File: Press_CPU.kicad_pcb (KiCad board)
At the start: 6 copper layers, 38.5 x 33 mm, 98 parts, among them J2 2-215079-0, J3 Conn_01x16, J4 Conn_01x16, U1 APM32F405RGT6, U10 LMV321, U11 LMV321, U12 FM25W256, U13 LMV321, U14 LMV321, U15 LMV321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

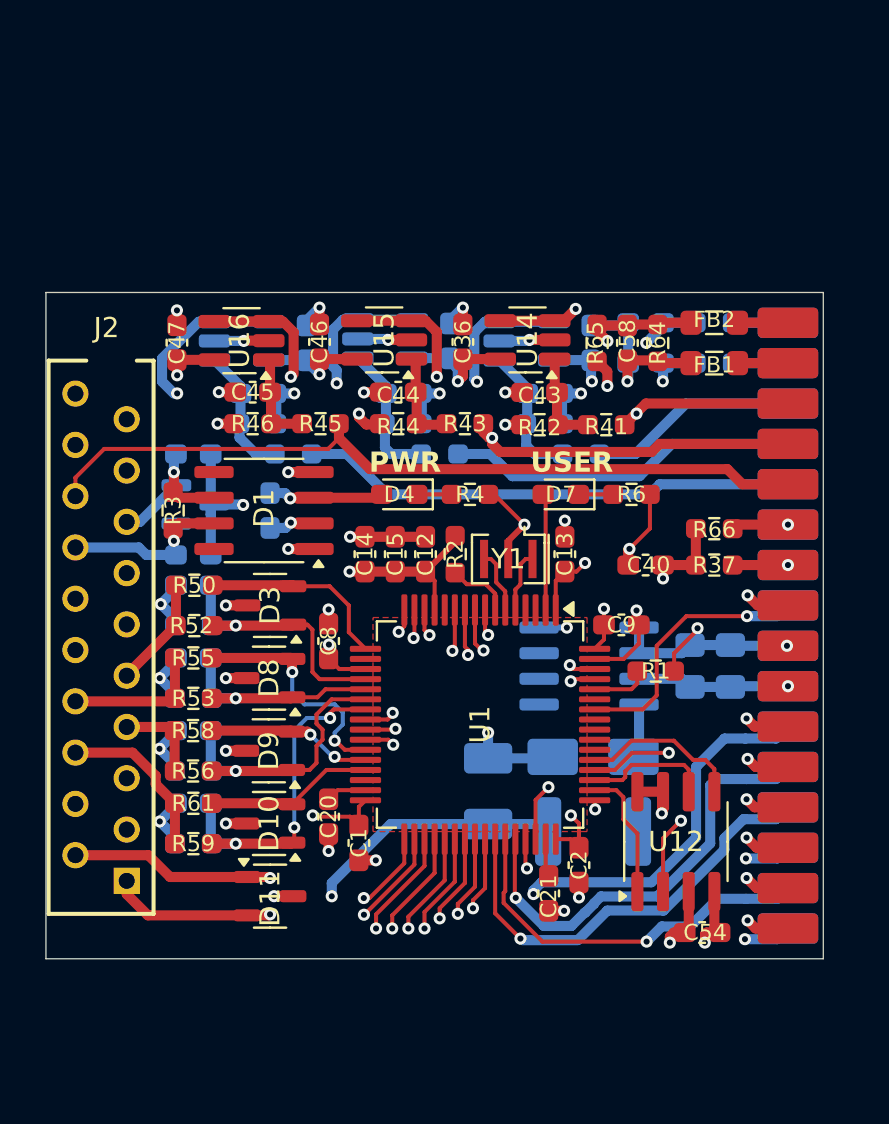
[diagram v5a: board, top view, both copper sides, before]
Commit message: VER1.0: добавил предохранители по питанию датчиков и внешнего CAN
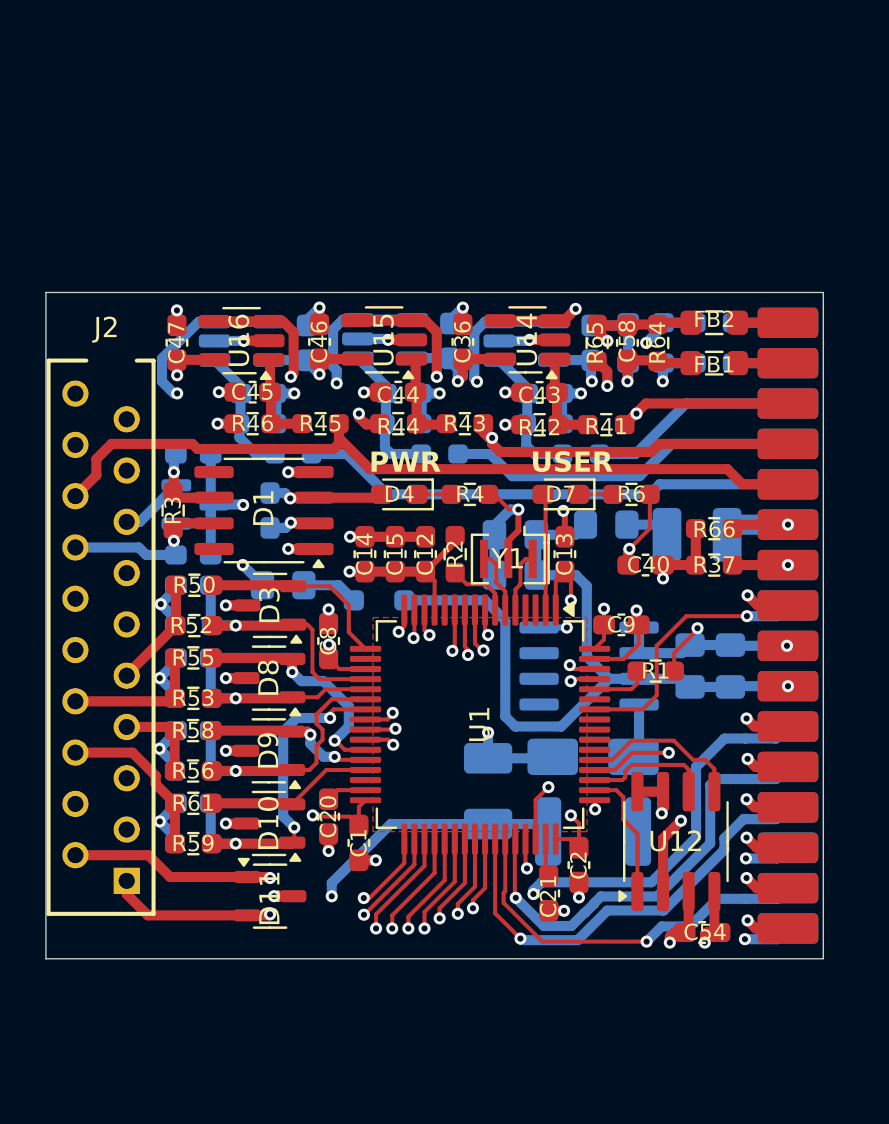
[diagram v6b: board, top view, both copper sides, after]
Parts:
- added C22: 10u, Capacitor_SMD:C_0805_2012Metric_Pad1.18x1.45mm_HandSolder, B.Cu at (149.8, 94.5)
- added C23: 10u, Capacitor_SMD:C_0805_2012Metric_Pad1.18x1.45mm_HandSolder, B.Cu at (149.8, 96.5)
- added D6: D_Schottky_Small, Diode_SMD:D_SOD-323_HandSoldering, B.Cu at (143.0, 97.8)
- added F1: Fuse_Small, Fuse:Fuse_0805_2012Metric_Pad1.15x1.40mm_HandSolder, B.Cu at (138.2, 97.0)
- added F2: Fuse_Small, Fuse:Fuse_0805_2012Metric_Pad1.15x1.40mm_HandSolder, B.Cu at (154.2, 94.0)
- added L2: 2.2u, Inductor_SMD:L_1210_3225Metric_Pad1.42x2.65mm_HandSolder, B.Cu at (158.8, 94.5)
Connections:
- J2 pad 10: +5V -> +5V_sense
- J2 pad 3: +5V -> +5V_sense
- J3 pad 6: +5V -> +5V_sense
- J4 pad 11: +5V -> +5V_sense
- R65 pad 1: +5V -> +5V_sense
- R66 pad 1: +5V -> +5V_sense
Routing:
- net +5V_sense: track 0.00 -> 63.6 mm, vias 0 -> 2
- net +5V: track 79.5 -> 38.0 mm, vias 3 -> 1
- net CAN_Power: track 0.00 -> 7.32 mm, vias 0 -> 1
- net GND: track 102.6 -> 107.1 mm
- net Net-(D6-K): track 0.00 -> 2.79 mm
- net BkIN: track 33.8 -> 31.3 mm
- net Net-(F2-Pad2): track 0.00 -> 2.19 mm
- net AnalogIN4_MCU: track 16.9 -> 17.7 mm
- removed copper zone on In1.Cu, net +3.3V
- removed copper zone on In2.Cu, net GND

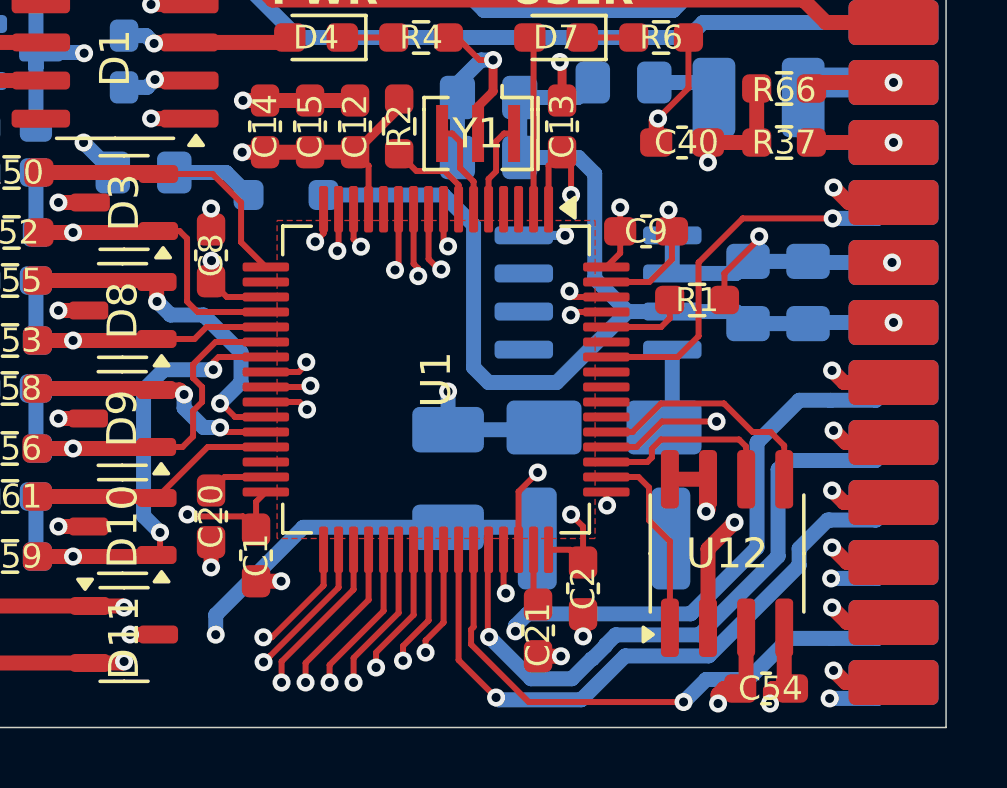
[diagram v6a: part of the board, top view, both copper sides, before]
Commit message: VER1.0: исправил дорожкт ШИМ
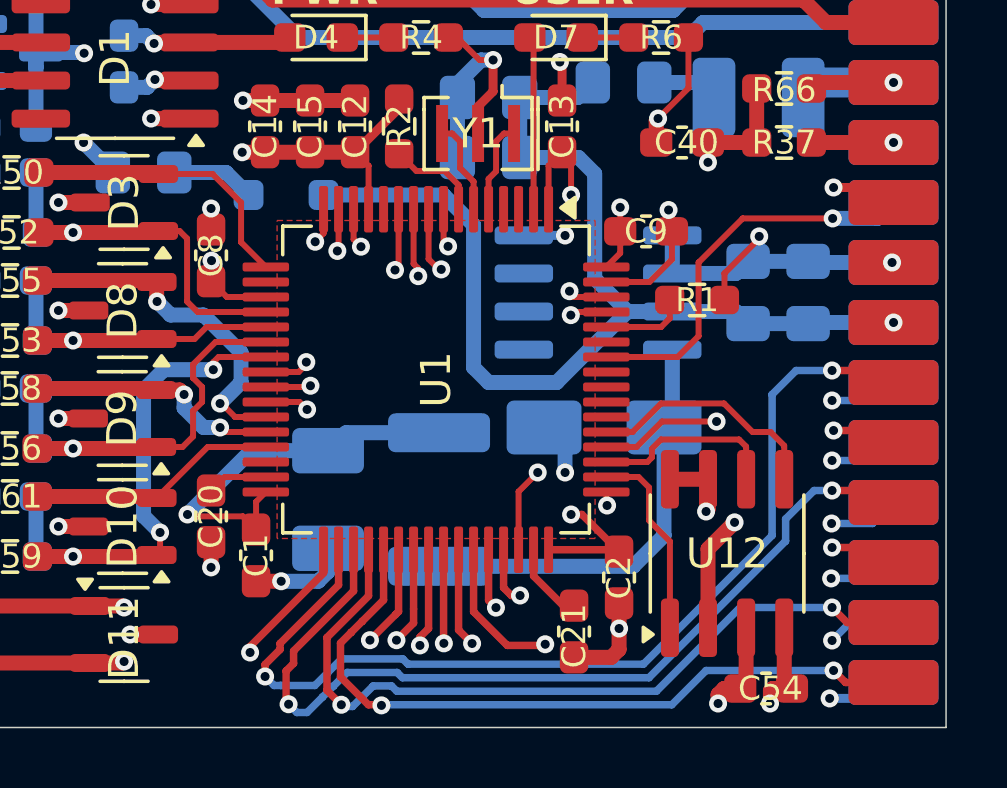
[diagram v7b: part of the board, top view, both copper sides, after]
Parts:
- moved L1 5.65 mm to (148.1, 107.9), turned to 90 degrees
- moved C19 4.06 mm to (144.4, 107.9), turned to -90 degrees
- moved C2 1.25 mm to (154.1, 110.5)
- moved C21 1.20 mm to (152.6, 112.3)
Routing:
- net Net-(D5-K): track 6.50 -> 14.6 mm
- net PWM1_L: track 30.0 -> 33.7 mm
- net f1H: track 22.1 -> 19.1 mm, vias 1 -> 2
- net PWM3_H: track 19.2 -> 16.9 mm, vias 1 -> 2
- net PWM2_H: track 21.8 -> 19.9 mm, vias 1 -> 2
- net +3.3V: track 66.3 -> 64.5 mm, vias 15 -> 14
- net BkIN: track 31.3 -> 33.2 mm
- net PWM2_L: track 28.7 -> 30.2 mm
- net GND: track 107.1 -> 108.6 mm, vias 42 -> 41
- net PWM1_H: track 25.5 -> 24.3 mm
- net f1L: track 17.0 -> 18.2 mm
- net f2H: track 24.3 -> 23.2 mm
- net Net-(U1-VCAP_2): track 1.89 -> 2.63 mm
- net f3H: track 23.9 -> 23.2 mm
- net f3L: track 25.0 -> 24.5 mm

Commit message: VER1.0: добавил шелкографию с версией
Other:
- board text added: "CPU VER1.0"
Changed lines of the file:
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@@
+		)
+	)
+	(gr_text "CPU VER1.0"
+		(at 127.25 115 0)
+		(layer "F.SilkS")
+		(effects
+			(font
+				(size 1 1)
+				(thickness 0.2)
+				(bold yes)
+			)
+			(justify left bottom)
 		)
 	)
